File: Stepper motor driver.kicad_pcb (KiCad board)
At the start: 2 copper layers, 35.8 x 35.8 mm, 16 parts, among them P1 CONN_01X04, P2 CONN_01X06, Q1 TIP120, Q2 TIP120, Q3 TIP120, Q4 TIP120, U1 74LS175, U2 74LS157

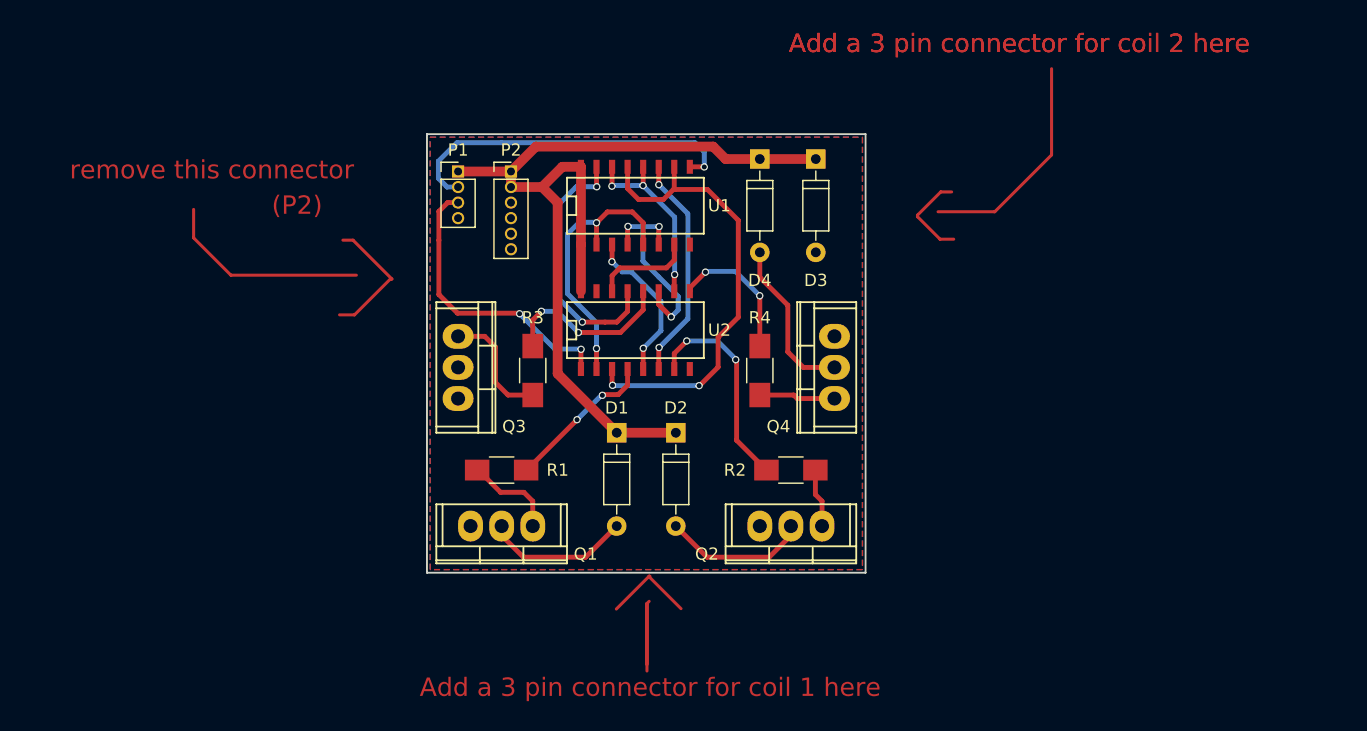
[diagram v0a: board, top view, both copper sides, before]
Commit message: Completed initial routing
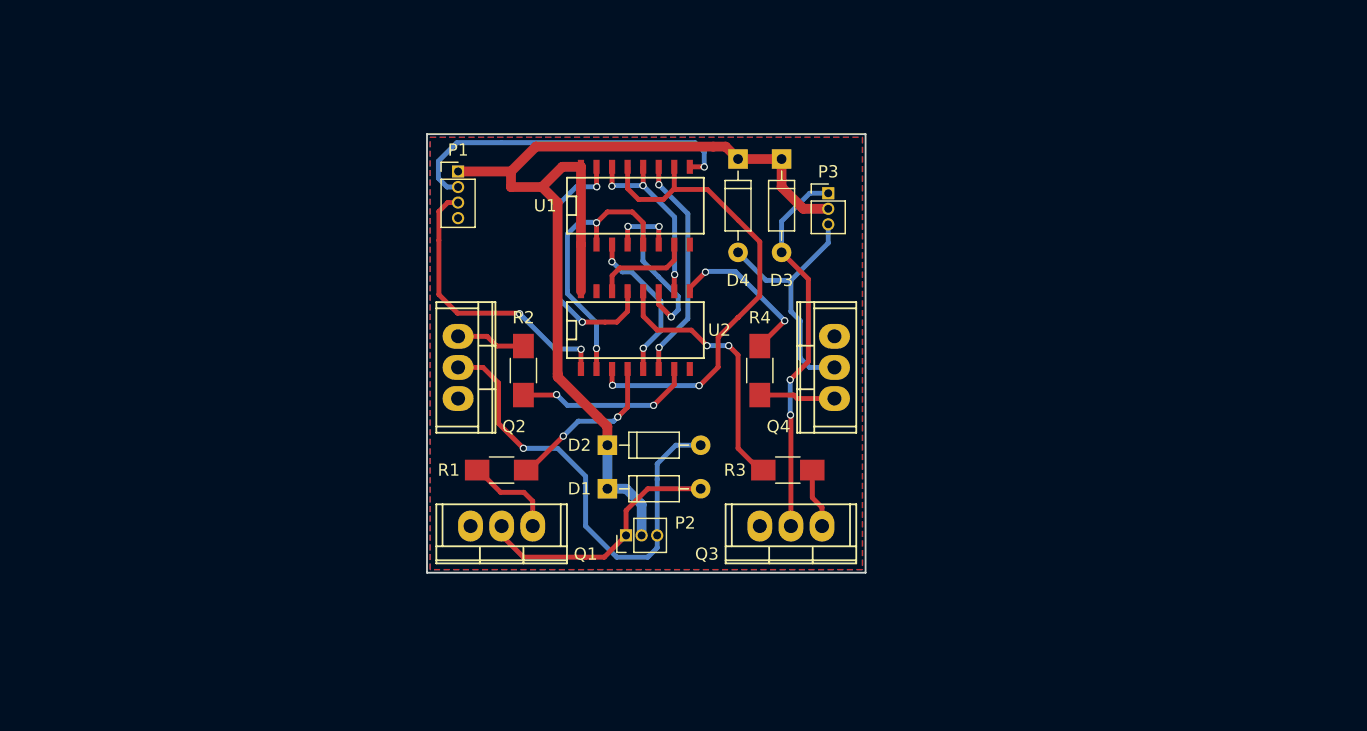
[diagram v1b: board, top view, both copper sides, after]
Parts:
- added P3: CONN_01X03, Pin_Headers:Pin_Header_Straight_1x03_Pitch1.27mm, F.Cu at (246.6, 122.4)
- P2: value CONN_01X06 -> CONN_01X03; footprint Pin_Headers:Pin_Header_Straight_1x06_Pitch1.27mm -> Pin_Headers:Pin_Header_Straight_1x03_Pitch1.27mm
- moved P2 31.2 mm to (230.1, 150.4), turned to 90 degrees
- moved Q2 30.1 mm to (216.4, 136.7), turned to 270 degrees
- moved Q3 30.1 mm to (243.6, 149.6), turned to 180 degrees
- moved R2 23.3 mm to (221.7, 136.9), turned to 270 degrees
- moved R3 22.4 mm to (243.3, 145.0), turned to 180 degrees
- moved D2 5.68 mm to (228.6, 143.0), turned to 0 degrees
- moved D1 4.64 mm to (228.6, 146.6), turned to 0 degrees
- moved D3 2.79 mm to (242.8, 119.6)
- moved D4 1.78 mm to (239.3, 119.6)
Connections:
- P2 pad 1: VCC -> /Coil1+
- P2 pad 3: /Coil1+ -> /Coil1-
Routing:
- net (no net): track 71.6 -> 0.00 mm
- net /Coil2+: track 0.00 -> 31.2 mm, vias 0 -> 2
- net /Coil1-: track 11.9 -> 38.3 mm, vias 0 -> 1
- net VCC: track 75.7 -> 85.0 mm
- net /Coil1+: track 11.9 -> 21.3 mm
- net /Coil2-: track 13.4 -> 20.9 mm
- net Net-(R3-Pad2): track 14.4 -> 21.5 mm
- net Net-(Q3-Pad1): track 9.77 -> 4.90 mm
- net Net-(R2-Pad2): track 17.4 -> 14.7 mm
- net Net-(R4-Pad2): track 11.5 -> 13.2 mm
- net /A2-: track 37.7 -> 39.2 mm
- net Net-(R1-Pad2): track 12.5 -> 13.6 mm
- net Net-(Q2-Pad1): track 4.80 -> 5.66 mm
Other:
- board text removed: "(P2)"
- board text removed: "Add a 3 pin connector for coil 1 here"
- board text removed: "Add a 3 pin connector for coil 2 here"
- board text removed: "remove this connector"

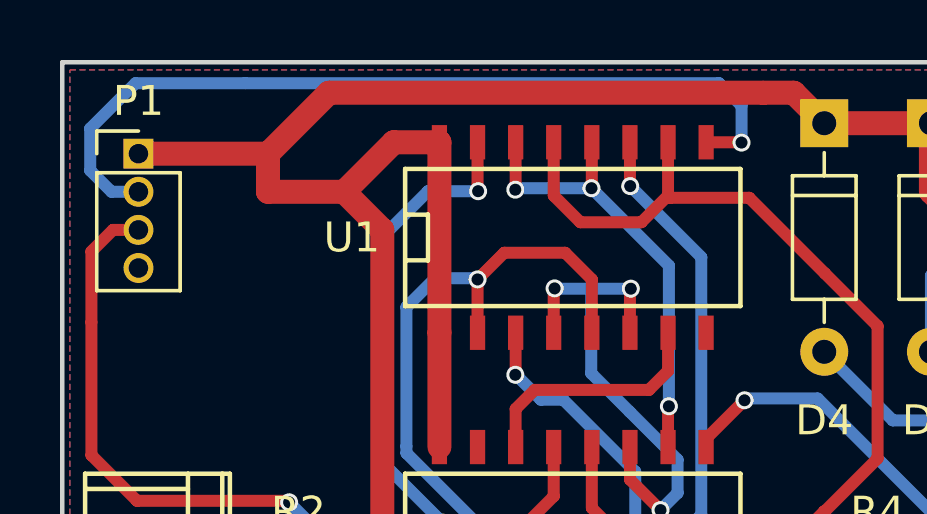
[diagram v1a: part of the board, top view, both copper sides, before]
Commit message: Moved input connector
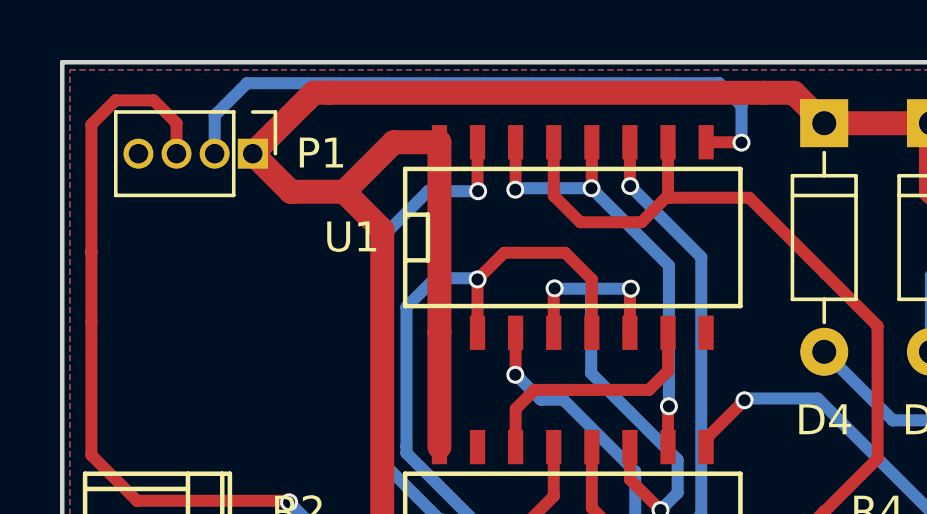
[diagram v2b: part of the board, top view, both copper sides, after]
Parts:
- moved P1 3.81 mm to (220.2, 120.7), turned to 270 degrees
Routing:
- net /DIR: track 23.7 -> 30.6 mm
- net /CLK: track 28.4 -> 22.0 mm
- net VCC: track 85.0 -> 81.0 mm
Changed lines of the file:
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@@
     (links 46)
     (no_connects 3)
-    (area 213.792999 117.526999 249.757001 153.491001)
+    (area 211.299667 112.466 259.968 155.476333)
     (thickness 1.6)
     (drawings 6)
-    (tracks 260)
+    (tracks 262)
     (zones 0)
     (modules 17)
@@
     (trace_clearance 0.2)
     (zone_clearance 0.508)
-    (zone_45_only no)
+    (zone_45_only yes)
     (trace_min 0.2)
     (segment_width 0.2)
@@
   )
   (module Pin_Headers:Pin_Header_Straight_1x04_Pitch1.27mm (layer F.Cu)
-    (at 216.408 120.65)
+    (at 220.218 120.65 270)
     (descr "Through hole straight pin header, 1x04, 1.27mm pitch, single row")
     (tags "Through hole pin header THT 1x04 1.27mm single row")
-    (fp_text reference P1 (at 0 -1.755) (layer F.SilkS)
-      (effects (font (size 1 1) (thickness 0.15)))
-    )
-    (fp_text value CONN_01X04 (at 0 5.565) (layer F.Fab)
+    (fp_text reference P1 (at 0 -2.286 360) (layer F.SilkS)
+      (effects (font (size 1 1) (thickness 0.15)))
+    )
+    (fp_text value CONN_01X04 (at 0 5.565 270) (layer F.Fab)
       (effects (font (size 1 1) (thickness 0.15)))
     )
@@
     (fp_line (start 1.6 4.7) (end 1.6 -0.9) (layer F.CrtYd) (width 0.05))
     (fp_line (start 1.6 -0.9) (end -1.6 -0.9) (layer F.CrtYd) (width 0.05))
-    (pad 1 thru_hole rect (at 0 0) (size 1 1) (drill 0.65) (layers *.Cu *.Mask)
+    (pad 1 thru_hole rect (at 0 0 270) (size 1 1) (drill 0.65) (layers *.Cu *.Mask)
       (net 19 VCC))
-    (pad 2 thru_hole oval (at 0 1.27) (size 1 1) (drill 0.65) (layers *.Cu *.Mask)
+    (pad 2 thru_hole oval (at 0 1.27 270) (size 1 1) (drill 0.65) (layers *.Cu *.Mask)
       (net 14 /CLK))
-    (pad 3 thru_hole oval (at 0 2.54) (size 1 1) (drill 0.65) (layers *.Cu *.Mask)
+    (pad 3 thru_hole oval (at 0 2.54 270) (size 1 1) (drill 0.65) (layers *.Cu *.Mask)
       (net 20 /DIR))
-    (pad 4 thru_hole oval (at 0 3.81) (size 1 1) (drill 0.65) (layers *.Cu *.Mask)
+    (pad 4 thru_hole oval (at 0 3.81 270) (size 1 1) (drill 0.65) (layers *.Cu *.Mask)
       (net 1 GND))
     (model Pin_Headers.3dshapes/Pin_Header_Straight_1x04_Pitch1.27mm.wrl
@@
   (segment (start 229.616 128.524) (end 233.426 128.524) (width 0.4) (layer F.Cu) (net 13))
   (segment (start 228.981 129.159) (end 229.616 128.524) (width 0.4) (layer F.Cu) (net 13))
-  (segment (start 216.408 121.92) (end 215.51 121.92) (width 0.4) (layer B.Cu) (net 14))
+  (segment (start 235.76 118.3) (end 220.028 118.3) (width 0.4) (layer B.Cu) (net 14))
+  (segment (start 235.331 120.269) (end 236.499 120.269) (width 0.4) (layer F.Cu) (net 14))
+  (segment (start 236.51 119.05) (end 235.76 118.3) (width 0.4) (layer B.Cu) (net 14))
+  (segment (start 236.51 120.28) (end 236.51 119.05) (width 0.4) (layer B.Cu) (net 14))
+  (via (at 236.51 120.28) (size 0.6) (drill 0.4) (layers F.Cu B.Cu) (net 14))
   (segment (start 236.499 120.269) (end 236.51 120.28) (width 0.4) (layer F.Cu) (net 14))
-  (via (at 236.51 120.28) (size 0.6) (drill 0.4) (layers F.Cu B.Cu) (net 14))
-  (segment (start 236.51 120.28) (end 236.51 119.05) (width 0.4) (layer B.Cu) (net 14))
-  (segment (start 236.51 119.05) (end 235.76 118.3) (width 0.4) (layer B.Cu) (net 14))
-  (segment (start 235.76 118.3) (end 219.97 118.3) (width 0.4) (layer B.Cu) (net 14))
-  (segment (start 236.499 120.269) (end 235.331 120.269) (width 0.4) (layer F.Cu) (net 14))
-  (segment (start 216.31 118.3) (end 219.97 118.3) (width 0.4) (layer B.Cu) (net 14))
-  (segment (start 214.8 119.81) (end 216.31 118.3) (width 0.4) (layer B.Cu) (net 14))
-  (segment (start 214.8 121.21) (end 214.8 119.81) (width 0.4) (layer B.Cu) (net 14))
-  (segment (start 215.51 121.92) (end 214.8 121.21) (width 0.4) (layer B.Cu) (net 14))
+  (segment (start 218.948 119.38) (end 218.948 120.65) (width 0.4) (layer B.Cu) (net 14) (status 800000))
+  (segment (start 220.028 118.3) (end 218.948 119.38) (width 0.4) (layer B.Cu) (net 14))
   (segment (start 239.26 132.58) (end 239.276 132.58) (width 0.4) (layer F.Cu) (net 15))
   (segment (start 234.134 122.12) (end 234.061 122.047) (width 0.4) (layer F.Cu) (net 15))
@@
   (segment (start 227.73 121.9) (end 227.711 121.881) (width 0.4) (layer F.Cu) (net 18))
   (via (at 227.73 121.9) (size 0.6) (drill 0.4) (layers F.Cu B.Cu) (net 18))
+  (segment (start 220.218 120.65) (end 221.488 121.92) (width 0.8) (layer F.Cu) (net 19) (status 400000))
+  (segment (start 221.488 121.92) (end 223.266 121.92) (width 0.8) (layer F.Cu) (net 19))
+  (segment (start 220.218 120.65) (end 221.996 118.872) (width 0.8) (layer F.Cu) (net 19) (status 400000))
+  (segment (start 238.252 118.618) (end 239.268 119.634) (width 0.8) (layer F.Cu) (net 19))
+  (segment (start 222.758 118.618) (end 237.236 118.618) (width 0.8) (layer F.Cu) (net 19))
+  (segment (start 237.236 118.618) (end 238.252 118.618) (width 0.8) (layer F.Cu) (net 19))
+  (segment (start 222.25 118.618) (end 222.758 118.618) (width 0.8) (layer F.Cu) (net 19))
+  (segment (start 221.996 118.872) (end 222.25 118.618) (width 0.8) (layer F.Cu) (net 19))
   (segment (start 242.824 119.634) (end 242.824 121.92) (width 0.8) (layer F.Cu) (net 19))
   (segment (start 244.602 123.698) (end 246.634 123.698) (width 0.8) (layer F.Cu) (net 19))
@@
   (segment (start 228.6 143.002) (end 228.6 146.558) (width 0.8) (layer B.Cu) (net 19))
   (segment (start 228.6 143.002) (end 228.6 141.478) (width 0.8) (layer F.Cu) (net 19))
+  (segment (start 228.6 141.478) (end 227.838 140.716) (width 0.8) (layer F.Cu) (net 19))
+  (segment (start 227.838 140.716) (end 224.536 137.414) (width 0.8) (layer F.Cu) (net 19))
+  (segment (start 224.536 137.414) (end 224.536 137.16) (width 0.8) (layer F.Cu) (net 19))
+  (segment (start 224.536 123.19) (end 223.266 121.92) (width 0.8) (layer F.Cu) (net 19))
   (segment (start 224.536 123.19) (end 224.536 137.16) (width 0.8) (layer F.Cu) (net 19))
-  (segment (start 224.536 123.19) (end 223.266 121.92) (width 0.8) (layer F.Cu) (net 19))
-  (segment (start 224.536 137.414) (end 224.536 137.16) (width 0.8) (layer F.Cu) (net 19))
-  (segment (start 227.838 140.716) (end 224.536 137.414) (width 0.8) (layer F.Cu) (net 19))
-  (segment (start 228.6 141.478) (end 227.838 140.716) (width 0.8) (layer F.Cu) (net 19))
   (segment (start 228.6 146.558) (end 230.124 146.558) (width 0.8) (layer B.Cu) (net 19))
   (segment (start 231.394 147.828) (end 230.124 146.558) (width 0.8) (layer B.Cu) (net 19))
   (segment (start 231.394 147.828) (end 231.394 150.368) (width 0.8) (layer B.Cu) (net 19))
   (segment (start 239.268 119.634) (end 242.824 119.634) (width 0.8) (layer F.Cu) (net 19))
-  (segment (start 237.236 118.618) (end 238.252 118.618) (width 0.8) (layer F.Cu) (net 19))
-  (segment (start 220.726 120.65) (end 222.758 118.618) (width 0.8) (layer F.Cu) (net 19))
-  (segment (start 222.758 118.618) (end 237.236 118.618) (width 0.8) (layer F.Cu) (net 19))
-  (segment (start 238.252 118.618) (end 239.268 119.634) (width 0.8) (layer F.Cu) (net 19))
-  (segment (start 216.408 120.65) (end 220.726 120.65) (width 0.8) (layer F.Cu) (net 19))
-  (segment (start 223.266 121.92) (end 220.726 121.92) (width 0.8) (layer F.Cu) (net 19))
   (segment (start 224.917 120.269) (end 226.441 120.269) (width 0.8) (layer F.Cu) (net 19))
   (segment (start 223.266 121.92) (end 224.917 120.269) (width 0.8) (layer F.Cu) (net 19))
   (segment (start 226.441 126.619) (end 226.441 120.269) (width 0.8) (layer F.Cu) (net 19))
   (segment (start 226.441 130.429) (end 226.441 126.619) (width 0.8) (layer F.Cu) (net 19))
-  (segment (start 220.726 121.92) (end 220.726 120.65) (width 0.8) (layer F.Cu) (net 19))
-  (segment (start 214.84 126.27) (end 214.84 123.91) (width 0.4) (layer F.Cu) (net 20))
+  (segment (start 214.84 123.952) (end 214.84 119.678) (width 0.4) (layer F.Cu) (net 20))
+  (segment (start 217.678 119.634) (end 217.678 120.65) (width 0.4) (layer F.Cu) (net 20) (status 800000))
+  (segment (start 216.916 118.872) (end 217.678 119.634) (width 0.4) (layer F.Cu) (net 20))
+  (segment (start 215.646 118.872) (end 216.916 118.872) (width 0.4) (layer F.Cu) (net 20))
+  (segment (start 214.84 119.678) (end 215.646 118.872) (width 0.4) (layer F.Cu) (net 20))
+  (segment (start 214.84 126.27) (end 214.84 123.952) (width 0.4) (layer F.Cu) (net 20))
+  (segment (start 214.84 123.952) (end 214.84 123.91) (width 0.4) (layer F.Cu) (net 20))
   (segment (start 221.43 132.27) (end 221.38 132.22) (width 0.4) (layer F.Cu) (net 20))
   (segment (start 221.38 132.22) (end 216.36 132.22) (width 0.4) (layer F.Cu) (net 20))
@@
   (segment (start 224.3 135.15) (end 224.3 135.14) (width 0.4) (layer B.Cu) (net 20))
   (via (at 221.43 132.27) (size 0.6) (drill 0.4) (layers F.Cu B.Cu) (net 20))
-  (segment (start 215.56 123.19) (end 216.408 123.19) (width 0.4) (layer F.Cu) (net 20))
-  (segment (start 214.84 123.91) (end 215.56 123.19) (width 0.4) (layer F.Cu) (net 20))
   (segment (start 236.22 146.558) (end 231.902 146.558) (width 0.4) (layer F.Cu) (net 21))
   (segment (start 230.124 148.336) (end 231.902 146.558) (width 0.4) (layer F.Cu) (net 21))

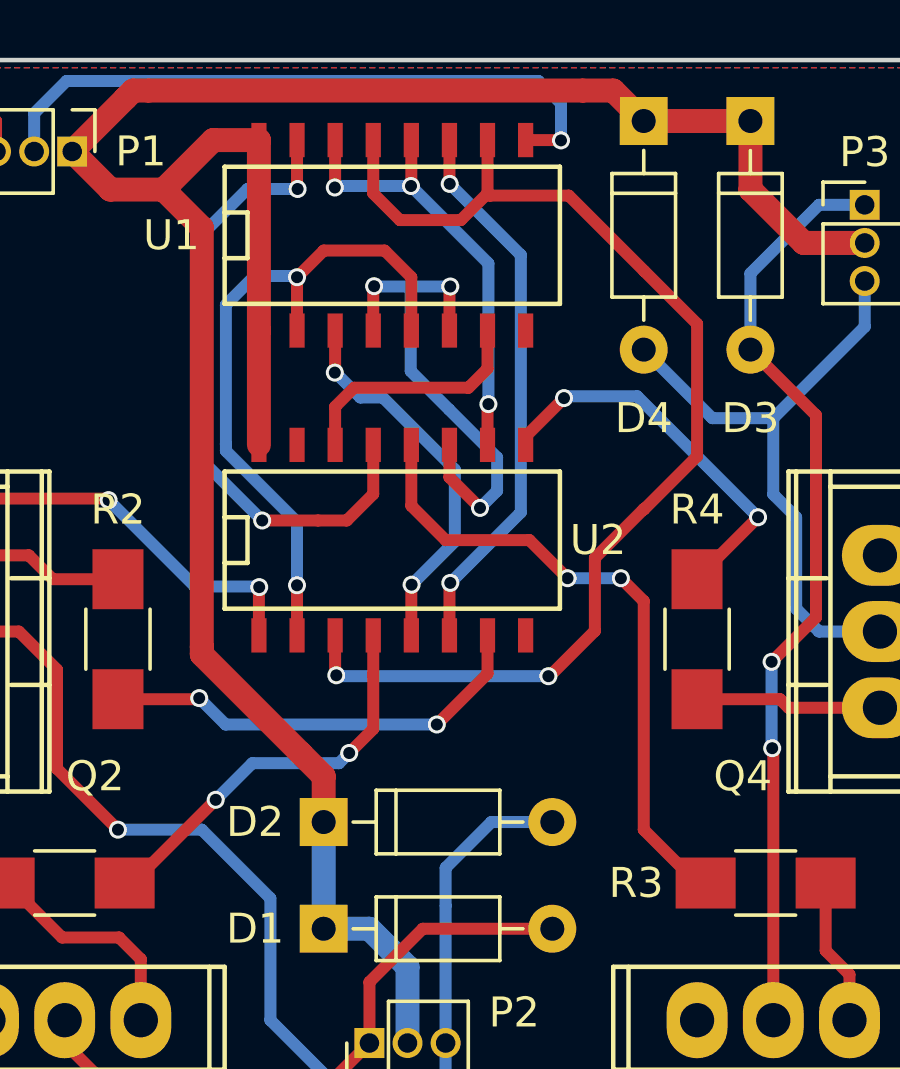
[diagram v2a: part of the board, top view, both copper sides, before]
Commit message: Refined traces to improve ground plane coverage
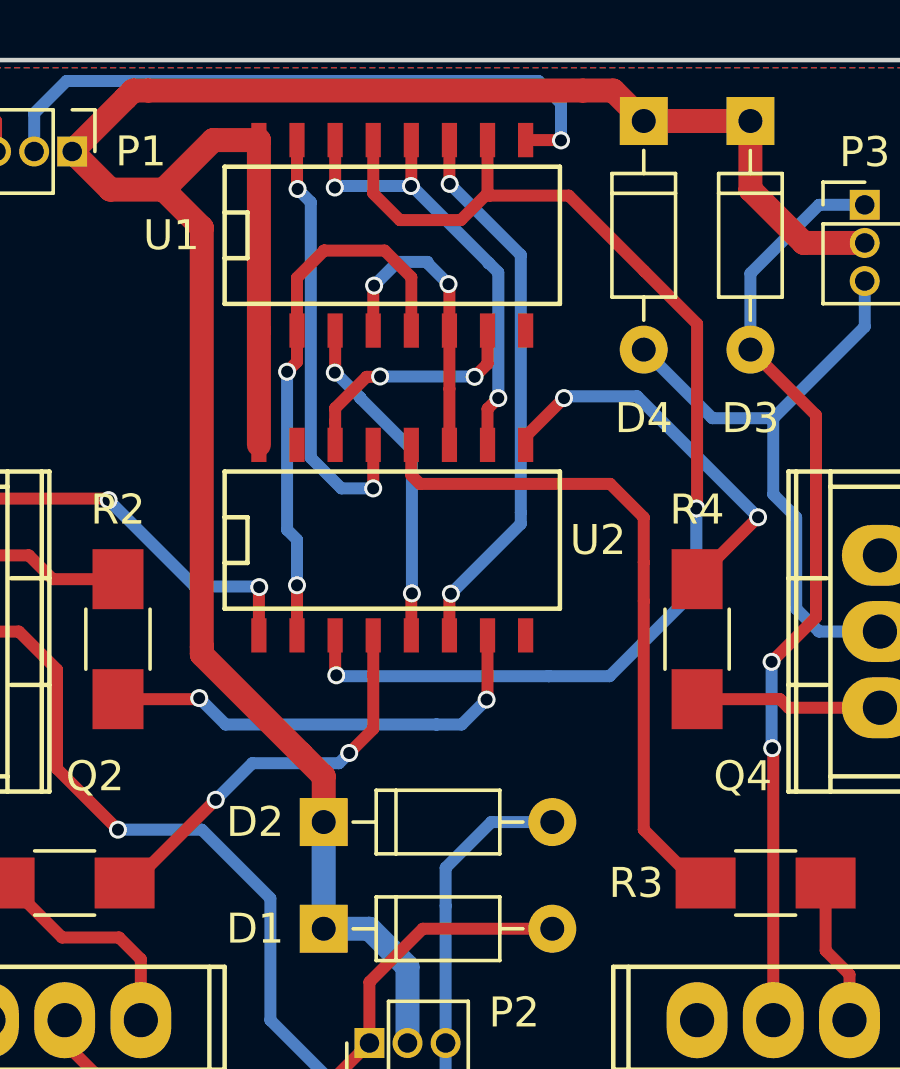
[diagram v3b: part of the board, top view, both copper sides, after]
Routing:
- net /A1+: track 16.8 -> 10.0 mm, vias 3 -> 2
- net /B2+: track 21.6 -> 14.7 mm
- net /B1+: track 22.9 -> 18.5 mm
- net /B1-: track 12.9 -> 11.2 mm
- net /A2-: track 39.2 -> 40.3 mm
- net Net-(R3-Pad2): track 21.5 -> 22.6 mm, vias 2 -> 0
- net /A1-: track 8.15 -> 8.03 mm, vias 0 -> 2
